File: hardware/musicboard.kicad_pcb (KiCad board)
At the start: 2 copper layers, 67.1 x 56.9 mm, 74 parts, among them J1 USB_B_Micro, J2 AudioJack3, J3 AudioJack3, J4 AudioJack3, J5 Conn_01x02_Female, J6 Conn_01x02_Female, J7 Conn_01x04_Female, J8 Conn_01x06_Female, SW1 SW_Push, U1 STM32F745VETx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

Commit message: add extension to board + add former fluidsynth
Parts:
- added D2: LED, LED_SMD:LED_0603_1608Metric_Pad1.05x0.95mm_HandSolder, F.Cu at (170.6, 108.0)
- added J9: Conn_01x03_Female, Connector_PinHeader_2.54mm:PinHeader_1x04_P2.54mm_Vertical, F.Cu at (109.2, 91.4)
- added R19: 1k, Resistor_SMD:R_0603_1608Metric_Pad1.05x0.95mm_HandSolder, F.Cu at (168.8, 104.5)
- J7: footprint Connector_PinHeader_2.54mm:PinHeader_1x04_P2.54mm_Vertical -> Connector_PinHeader_2.54mm:PinHeader_1x08_P2.54mm_Vertical
- moved J7 9.40 mm to (129.5, 113.8)
- moved C33 2.29 mm to (115.6, 85.3)
- moved D1 1.40 mm to (170.6, 109.6)
- moved R1 1.40 mm to (170.2, 95.6)
- moved C4 1.02 mm to (146.6, 103.9)
- moved J5 1.02 mm to (170.7, 99.1)
- moved C34 0.76 mm to (123.2, 85.3)
- moved C5 0.72 mm to (162.6, 109.0)
- moved C6 0.65 mm to (146.6, 105.9)
- moved R17 0.28 mm to (168.8, 106.2)
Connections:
- net /LED renamed /LED1
- J7 pad 2: /TX -> /EXT_SCL
- J7 pad 3: /RX -> /EXT_SDA
- J7 pad 4: GND -> /TX2
- U1 pad 46: Net-(U1-Pad46) -> /EXT_SCL
- U1 pad 47: Net-(U1-Pad47) -> /EXT_SDA
- U1 pad 63: /TX -> /TX1
- U1 pad 64: /RX -> /RX1
- U1 pad 78: Net-(U1-Pad78) -> /TX2
- U1 pad 79: Net-(U1-Pad79) -> /RX2
- U1 pad 80: Net-(U1-Pad80) -> /LED2
- U4 pad 17: Net-(U4-Pad17) -> /MICBIAS
- U4 pad 18: Net-(U4-Pad18) -> /MICIN
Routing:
- net /TX2: track 0.00 -> 35.5 mm, vias 0 -> 1
- net /RX2: track 0.00 -> 32.0 mm, vias 0 -> 1
- net /EXT_SCL: track 0.00 -> 23.6 mm, vias 0 -> 1
- net /TX: track 20.4 -> 0.00 mm, vias 1 -> 0
- net /EXT_SDA: track 0.00 -> 20.4 mm, vias 0 -> 1
- net /TX1: track 0.00 -> 19.6 mm, vias 0 -> 1
- net /RX: track 18.6 -> 0.00 mm, vias 1 -> 0
- net /RX1: track 0.00 -> 17.9 mm, vias 0 -> 1
- net /MICBIAS: track 0.00 -> 17.8 mm, vias 0 -> 1
- net /MICIN: track 0.00 -> 16.5 mm, vias 0 -> 1
- net Net-(D2-Pad2): track 0.00 -> 4.16 mm
- net /LED2: track 0.00 -> 3.73 mm
- net /QSPI_D3: track 26.1 -> 29.5 mm
- net /VDDA: track 38.6 -> 41.8 mm
- net Net-(D1-Pad2): track 1.79 -> 4.12 mm
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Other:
- board text added: "GNDA"
- board text added: "IO0/SCL"
- board text added: "IO1/SDA"
- board text added: "IO2/TX"
- board text added: "IO3/RX"
- board text added: "IO4/TX"
- board text added: "IO5/RX"
- board text added: "MICBIAS"
- board text added: "MICIN"
- board text added: "rev 2 2020-06-12"
- board text removed: "RX"
- board text removed: "TX"
- board text removed: "rev 1 2020-06-10"

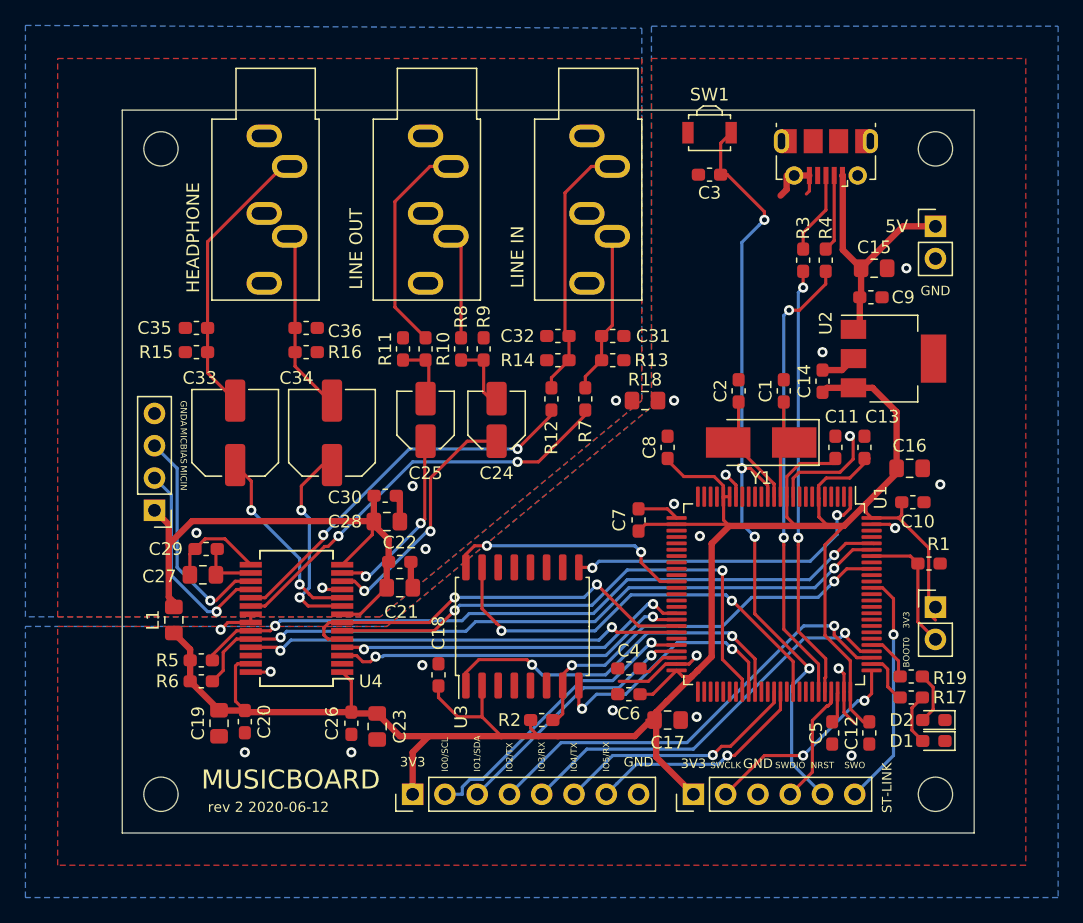
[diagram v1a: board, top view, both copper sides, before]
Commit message: use usb mini b + add usb header
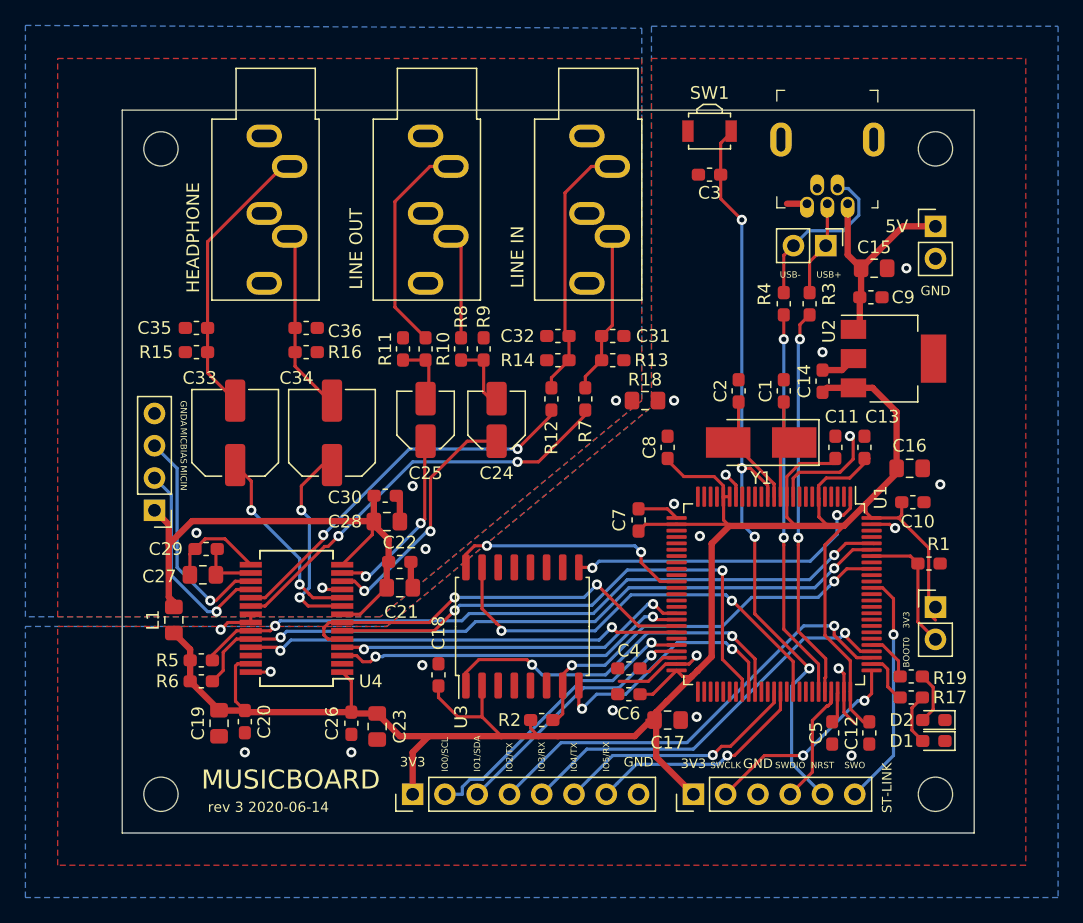
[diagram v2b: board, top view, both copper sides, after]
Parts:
- added J10: Conn_01x02_Female, Connector_PinHeader_2.54mm:PinHeader_1x02_P2.54mm_Vertical, F.Cu at (162.1, 70.6)
- J1: value USB_B_Micro -> USB_B_Mini; footprint Connector_USB:USB_Micro-B_Molex-105017-0001 -> hardware:USB-mini-B-0548190519
- J9: value Conn_01x03_Female -> Conn_01x04_Female
- moved R4 4.76 mm to (158.8, 75.2)
- moved J1 3.68 mm to (162.2, 67.3), turned to 270 degrees
- moved R3 3.47 mm to (160.8, 75.2)
- moved SW1 0.13 mm to (152.9, 61.6)
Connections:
- net Net-(J1-Pad2) renamed /DM
- net Net-(J1-Pad3) renamed /DP
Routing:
- net /DM: track 6.07 -> 13.4 mm
- net /USB_DM: track 36.1 -> 30.8 mm
- net /USB_DP: track 34.2 -> 30.9 mm
- net GND: track 39.8 -> 36.8 mm
- net +5V: track 20.2 -> 17.8 mm
- net /NRST: track 62.5 -> 60.7 mm
- net /DP: track 6.53 -> 7.58 mm
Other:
- board text added: "USB+"
- board text added: "USB-"
- board text added: "rev 3 2020-06-14"
- board text removed: "rev 2 2020-06-12"

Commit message: add vdda
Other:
- board text added: "VDDA"
